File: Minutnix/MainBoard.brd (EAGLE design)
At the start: 222.3 x 73.3 mm, 120 parts, among them IC3 TP4056, IC7 FT232RL, Q4 32.768kHz, X1 FH12-12S-0.5S_THINNER, X2 JST-XH-03-PIN-LONG-PAD, X4 JST-XH-03-PIN-LONG-PAD

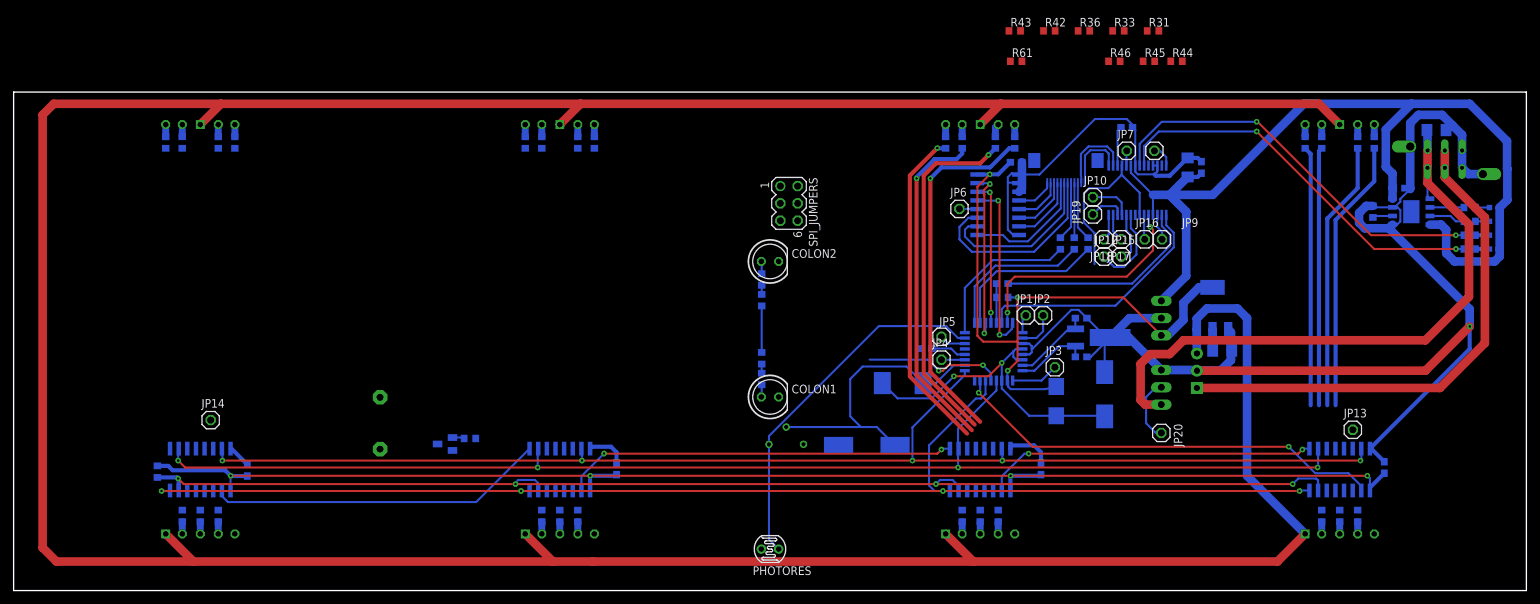
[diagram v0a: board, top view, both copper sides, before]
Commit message: PCB with original pinout
Register inputs unconnected but drawn close
Not every path has optimal width
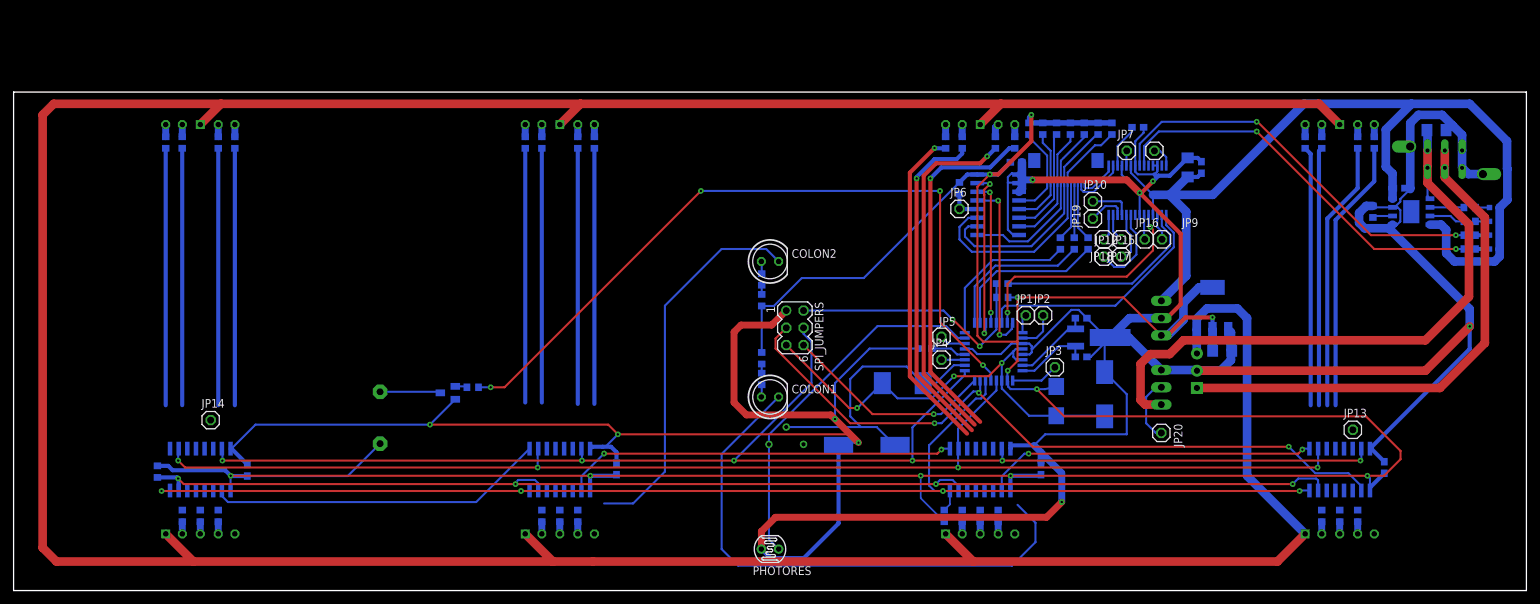
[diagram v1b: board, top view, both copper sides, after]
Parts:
- moved R36 74.2 mm to (136.8, 11.0), flipped to the bottom, turned to 270 degrees
- moved R61 20.4 mm to (139.0, 59.1), flipped to the bottom, turned to 270 degrees
- moved R44 20.2 mm to (153.3, 67.9), flipped to the bottom, turned to 270 degrees
- moved R45 18.5 mm to (151.2, 67.9), flipped to the bottom, turned to 270 degrees
- moved SPI_JUMPERS 18.3 mm to (114.8, 38.6)
- moved R43 16.5 mm to (155.3, 67.9), flipped to the bottom, turned to 270 degrees
- moved R46 16.0 mm to (149.2, 67.9), flipped to the bottom, turned to 270 degrees
- moved R31 15.6 mm to (161.4, 67.9), flipped to the bottom, turned to 270 degrees
- moved R42 15.3 mm to (157.3, 67.9), flipped to the bottom, turned to 270 degrees
- moved R33 14.7 mm to (159.4, 67.9), flipped to the bottom, turned to 270 degrees
- moved R30 7.53 mm to (67.5, 29.9)
- moved Q2 7.53 mm to (63.8, 29.1)
- moved C1 1.63 mm to (165.2, 68.1)
- moved SG1 0.81 mm to (53.8, 25.4)
- moved JP10 0.61 mm to (158.6, 57.2)
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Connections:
- removed net GNDA: ATMEGA328P.21, PHOTORES.1
- net GND: now also ATMEGA328P.21, PHOTORES.1
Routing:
- net GND: track 305.7 -> 598.3 mm, vias 1 -> 9
- net VCC: track 306.2 -> 476.0 mm, vias 7 -> 11
- net BUZZ: track 20.4 -> 110.7 mm, vias 2 -> 4
- net N$2: track 0.00 -> 81.0 mm
- net N$20: track 0.00 -> 56.2 mm
- net D_SI: track 64.4 -> 104.7 mm, vias 2 -> 3
- net N$96: track 0.00 -> 37.8 mm
- net N$75: track 0.00 -> 37.8 mm
- net N$22: track 0.00 -> 37.8 mm
- net N$95: track 0.00 -> 37.7 mm
- net N$68: track 0.00 -> 37.6 mm
- net N$67: track 0.00 -> 37.6 mm
- net N$73: track 0.00 -> 37.4 mm
- net N$72: track 0.00 -> 37.4 mm
- net RESET: track 5.77 -> 38.3 mm, vias 0 -> 2
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
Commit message: Final packages
+most paths wider (24 mils)
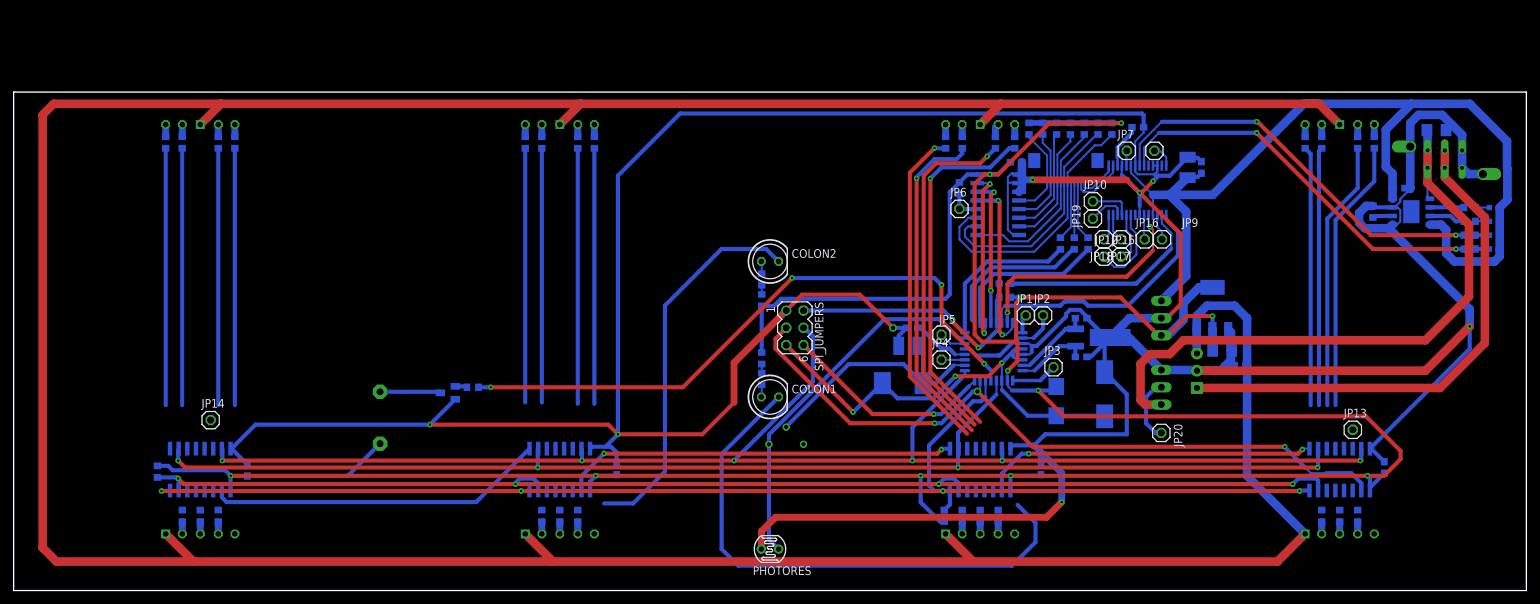
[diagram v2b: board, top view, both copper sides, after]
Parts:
- removed C5SPRAWDZGOOOOOOOOOOOOOOOOOOOOOOOOOOOOOOOOOOOOOOOOOOO, C5SPRAWDZGOOOOOOOOOOOOOOOOOOOOOOOOOOOOOOOOOOOOOOOOOOO1: 10u, rcl:C3216
- added C6: 100n, rcl:C0603
- added C7, C8: 10u, rcl:C1206
- C3: device rcl:C3216 -> rcl:SMC_B
- C32: device rcl:140CLH-1010 -> rcl:C1210
- R39, R40, R47, R52, R64, R65, R66: value 620R-1k -> 820R
- moved C32 15.8 mm to (131.5, 36.0), turned to 0 degrees
- moved C4 3.66 mm to (132.1, 38.6)
- moved C10 0.41 mm to (145.7, 45.1)
- moved R56 0.41 mm to (145.7, 43.1)
- moved JP5 0.30 mm to (136.3, 37.6)
- moved JP3 0.20 mm to (152.8, 32.8)
- renumbered U$2 to SWITCH
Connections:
- net +5V: now also C3.+; no longer C3.1
- net AVCC: now also C32.1; no longer C32.+
- net BATTERY+: now also C8.2; no longer C5SPRAWDZGOOOOOOOOOOOOOOOOOOOOOOOOOOOOOOOOOOOOOOOOOOO1.2
- net GND: now also C3.-, C32.2, C6.1, C7.2, C8.1; no longer C3.2, C32.-, C5SPRAWDZGOOOOOOOOOOOOOOOOOOOOOOOOOOOOOOOOOOOOOOOOOOO.2, C5SPRAWDZGOOOOOOOOOOOOOOOOOOOOOOOOOOOOOOOOOOOOOOOOOOO1.1
- net VCC: now also C7.1; no longer C5SPRAWDZGOOOOOOOOOOOOOOOOOOOOOOOOOOOOOOOOOOOOOOOOOOO.1
- net VDD: now also C6.2
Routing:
- net GND: track 598.3 -> 652.6 mm, vias 9 -> 8
- net VCC: track 476.0 -> 508.4 mm
- net BUZZ: track 110.7 -> 92.2 mm
- net AVCC: track 44.5 -> 38.2 mm
- net AREF: track 5.17 -> 8.47 mm
- net RXD: track 36.3 -> 38.4 mm
- net LIGHT_SENS: track 53.5 -> 54.4 mm
- net EXP_SCL: track 21.1 -> 21.9 mm
- net VDD: track 523.3 -> 524.1 mm
- net S_VCC: track 66.9 -> 67.6 mm
- net RESET: track 38.3 -> 38.9 mm
- net L_WARNING: track 22.2 -> 22.8 mm

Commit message: Mixing led signals
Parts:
- moved JP14 14.5 mm to (32.8, 11.0)
- moved JP13 12.0 mm to (199.8, 12.0)
- moved MS_MIN_REG 0.81 mm to (28.2, 17.8)
- moved R29 0.81 mm to (21.9, 17.5)
- moved C15 0.81 mm to (35.2, 17.7)
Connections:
- net N$10 renamed LS_F
- net N$62 renamed MS_F
- net N$72 renamed LM_F
- net N$95 renamed MM_F
- removed net N$11: LS_SEC_REG.13, R15.2
- removed net N$2: COLON1.K, MS_SEC_REG.14
- removed net N$20: COLON2.K, LS_MIN_REG.14
- removed net N$22: MS_MIN_REG.3, R27.2
- removed net N$4: MS_SEC_REG.3, R14.2
- removed net N$5: LS_SEC_REG.3, R21.2
- removed net N$58: MS_SEC_REG.4, R13.2
- removed net N$59: MS_SEC_REG.5, R12.2
- removed net N$6: LS_SEC_REG.4, R20.2
- removed net N$60: MS_SEC_REG.6, R11.2
- removed net N$61: MS_SEC_REG.11, R10.2
- removed net N$63: MS_SEC_REG.13, R8.2
- removed net N$67: LS_MIN_REG.3, R7.2
- removed net N$68: LS_MIN_REG.4, R6.2
- removed net N$69: LS_MIN_REG.5, R5.2
- removed net N$7: LS_SEC_REG.5, R19.2
- removed net N$70: LS_MIN_REG.6, R4.2
- removed net N$71: LS_MIN_REG.11, R3.2
- removed net N$73: LS_MIN_REG.13, R1.2
- removed net N$75: MS_MIN_REG.4, R26.2
- removed net N$76: MS_MIN_REG.5, R25.2
- removed net N$77: MS_MIN_REG.6, R24.2
- removed net N$8: LS_SEC_REG.6, R18.2
- removed net N$9: LS_SEC_REG.11, R17.2
- removed net N$94: MS_MIN_REG.11, R23.2
- removed net N$96: MS_MIN_REG.13, R28.2
- new net COL_1: COLON1.K, MS_SEC_REG.3
- new net COL_2: COLON2.K, LS_MIN_REG.3
- new net LM_A: LS_MIN_REG.13, R7.2
- new net LM_B: LS_MIN_REG.14, R6.2
- new net LM_C: LS_MIN_REG.4, R5.2
- new net LM_D: LS_MIN_REG.5, R4.2
- new net LM_E: LS_MIN_REG.6, R3.2
- new net LM_G: LS_MIN_REG.11, R1.2
- new net LS_A: LS_SEC_REG.13, R21.2
- new net LS_B: LS_SEC_REG.14, R20.2
- new net LS_C: LS_SEC_REG.4, R19.2
- new net LS_D: LS_SEC_REG.5, R18.2
- new net LS_E: LS_SEC_REG.6, R17.2
- new net LS_G: LS_SEC_REG.11, R15.2
- new net MM_A: MS_MIN_REG.13, R27.2
- new net MM_B: MS_MIN_REG.14, R26.2
- new net MM_C: MS_MIN_REG.4, R25.2
- new net MM_D: MS_MIN_REG.5, R24.2
- new net MM_E: MS_MIN_REG.6, R23.2
- new net MM_G: MS_MIN_REG.11, R28.2
- new net MS_A: MS_SEC_REG.13, R14.2
- new net MS_B: MS_SEC_REG.14, R13.2
- new net MS_C: MS_SEC_REG.4, R12.2
- new net MS_D: MS_SEC_REG.5, R11.2
- new net MS_E: MS_SEC_REG.6, R10.2
- new net MS_G: MS_SEC_REG.11, R8.2
- net UD1: now also LS_SEC_REG.3; no longer LS_SEC_REG.14
- net UD2: now also MS_MIN_REG.3; no longer MS_MIN_REG.14
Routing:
- net COL_1: track 0.00 -> 84.1 mm
- net N$2: track 81.0 -> 0.00 mm
- net COL_2: track 0.00 -> 61.4 mm
- net MS_B: track 0.00 -> 58.2 mm, vias 0 -> 2
- net N$20: track 56.2 -> 0.00 mm
- net MS_A: track 0.00 -> 56.0 mm, vias 0 -> 2
- net N$58: track 53.0 -> 0.00 mm, vias 1 -> 0
- net N$4: track 51.9 -> 0.00 mm, vias 1 -> 0
- net MS_G: track 0.00 -> 51.0 mm, vias 0 -> 2
- net N$63: track 48.6 -> 0.00 mm, vias 1 -> 0
- net LS_B: track 0.00 -> 46.0 mm
- net MM_G: track 0.00 -> 45.8 mm
- net LS_A: track 0.00 -> 45.5 mm
- net LM_G: track 0.00 -> 45.4 mm
- net LM_B: track 0.00 -> 45.4 mm
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
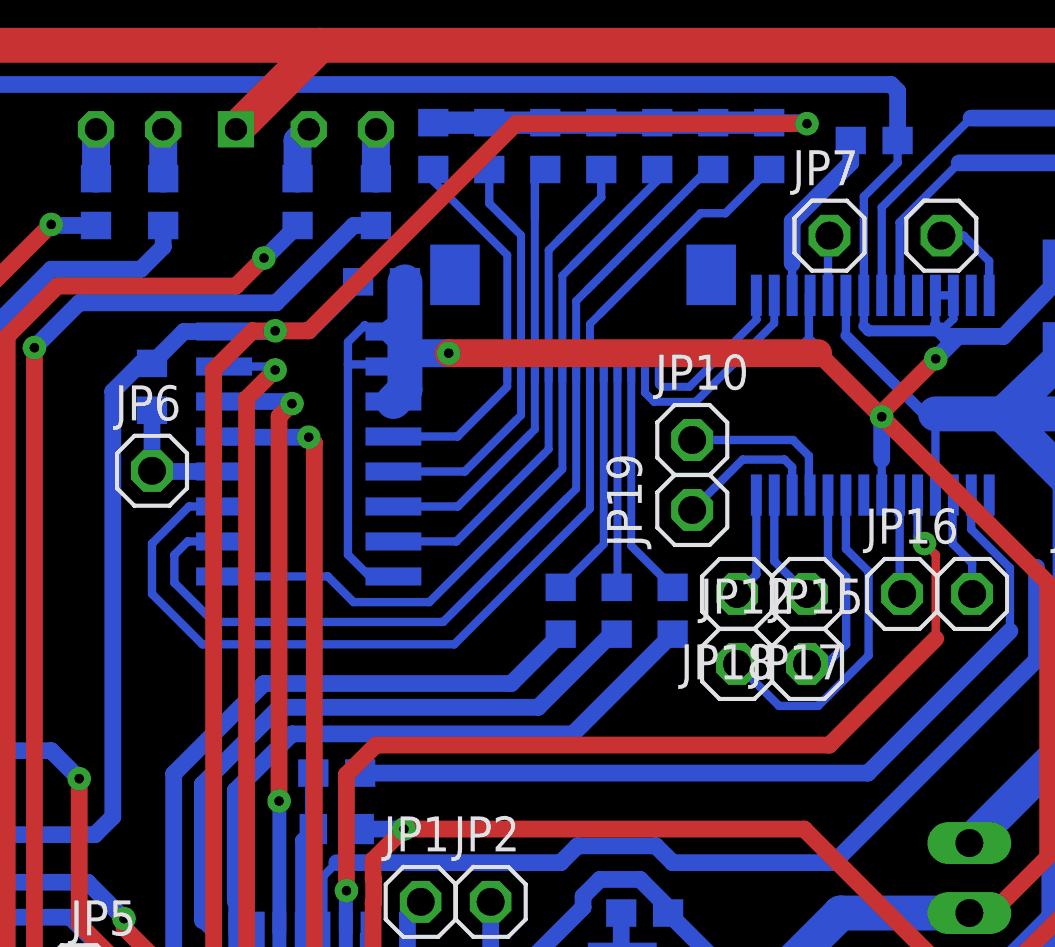
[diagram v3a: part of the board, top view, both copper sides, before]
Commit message: rotation of tape ports
also some nets wider
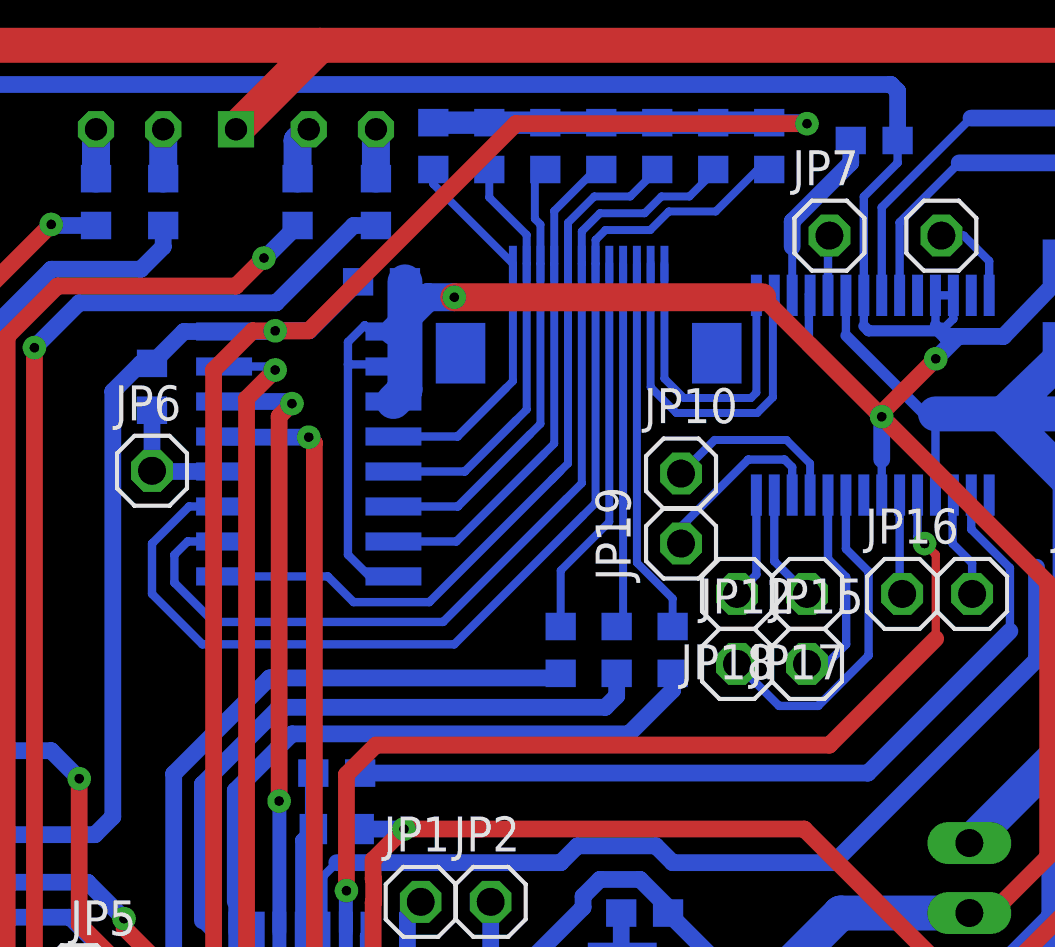
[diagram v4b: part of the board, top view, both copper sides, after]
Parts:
- moved X1 2.85 mm to (154.8, 60.4), turned to 0 degrees
- moved R47 1.42 mm to (155.9, 49.6)
- moved R52 1.42 mm to (153.8, 49.6)
- moved R64 1.42 mm to (157.9, 49.6)
- moved JP10 1.29 mm to (158.2, 56.0)
- moved JP19 1.29 mm to (158.2, 53.4)
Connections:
- removed net N$12: R64.1, X1.10
- removed net N$26: R47.1, X1.9
- removed net N$28: R52.1, X1.8
- new net N$20: R64.1, X1.3
- new net N$22: R47.1, X1.4
- new net N$30: R52.1, X1.5
- net COUNTER: now also X1.10; no longer X1.3
- net ENC_A: now also X1.7; no longer X1.6
- net ENC_B: now also X1.6; no longer X1.7
- net PLAY/PAUSE: now also X1.11; no longer X1.2
- net STOP/RESET: now also X1.12; no longer X1.1
- net USBDM: now also X1.2; no longer X1.11
- net USBDP: now also X1.1; no longer X1.12
- net VOLUME: now also X1.8; no longer X1.5
- net WARNING: now also X1.9; no longer X1.4
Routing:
- net N$30: track 0.00 -> 13.9 mm
- net N$20: track 0.00 -> 13.7 mm
- net N$22: track 0.00 -> 13.3 mm
- net N$28: track 8.74 -> 0.00 mm
- net N$12: track 8.71 -> 0.00 mm
- net N$26: track 8.10 -> 0.00 mm
- net USBDM: track 8.05 -> 13.3 mm
- net USBDP: track 6.20 -> 11.4 mm
- net ENC_B: track 39.2 -> 40.9 mm
- net ENC_A: track 34.0 -> 35.4 mm
- net CBUS4: track 5.51 -> 6.78 mm
- net VOLUME: track 27.0 -> 28.2 mm
- net GND: track 653.3 -> 654.3 mm
- net CTS: track 5.91 -> 6.69 mm
- net L_COUNTER: track 23.3 -> 22.7 mm
